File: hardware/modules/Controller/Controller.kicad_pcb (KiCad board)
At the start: 2 copper layers, 120 x 72 mm, 86 parts, among them J1 DEBUG, J2 Conn_01x04_MountingPin, J3 Jumper, J4 Conn_01x04_MountingPin, SW1 RESET, SW10 sw1, SW2 BOOT0, SW3 sw1, SW5 sw1, SW6 sw1, SW7 sw1, SW8 sw1, SW9 sw1, U1 SN65HVD230, U2 W25Q128JVS, U3 RP2040, Y1 Crystal_GND24

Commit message: 主にControllerの更新です
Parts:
- J2, J4: moved to F.Cu
- moved R1 56.5 mm to (122.3, 79.7)
- moved C12 56.5 mm to (110.9, 89.2)
- moved R12 56.4 mm to (121.2, 88.1)
- moved C11 56.4 mm to (121.2, 89.1)
- moved C15 56.4 mm to (111.0, 84.9)
- moved C3 56.4 mm to (113.5, 97.4)
- moved D2 56.4 mm to (112.1, 80.8)
- moved D3 56.4 mm to (116.1, 80.8)
- moved D4 56.4 mm to (118.2, 80.8)
- moved R10 56.4 mm to (122.5, 75.9)
- moved R4 56.4 mm to (114.3, 80.9)
- moved R9 56.4 mm to (118.0, 94.5)
- moved U1 56.4 mm to (127.0, 77.9)
- moved USB1 56.4 mm to (116.2, 75.1)
- moved C1 56.4 mm to (122.5, 77.8)
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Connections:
- C16 pad 2: /ModuleIF/VIO -> VDD
- J4 pad 3: /ModuleIF/VIO -> VDD
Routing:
- net GND: track 159.0 -> 433.7 mm, vias 12 -> 276
- net VDD: track 92.8 -> 323.5 mm
- net /raw2: track 0.00 -> 132.1 mm, vias 0 -> 5
- net /raw1: track 0.00 -> 125.7 mm, vias 0 -> 3
- net /raw4: track 0.00 -> 116.8 mm, vias 0 -> 1
- net Net-(lcd1-K): track 0.00 -> 116.1 mm, vias 0 -> 1
- net /raw3: track 0.00 -> 114.7 mm, vias 0 -> 1
- net /NoGo: track 0.00 -> 103.9 mm, vias 0 -> 4
- net /abort: track 0.00 -> 103.3 mm, vias 0 -> 4
- net /Go: track 0.00 -> 102.4 mm, vias 0 -> 4
- net /sub: track 0.00 -> 93.2 mm, vias 0 -> 5
- net /col4: track 0.00 -> 93.1 mm, vias 0 -> 2
- net /col3: track 0.00 -> 86.5 mm, vias 0 -> 2
- net /col2: track 0.00 -> 81.6 mm, vias 0 -> 2
- net /col1: track 0.00 -> 77.0 mm, vias 0 -> 2
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- added copper zone on B.Cu, net GND
- added copper zone on F.Cu, net GND

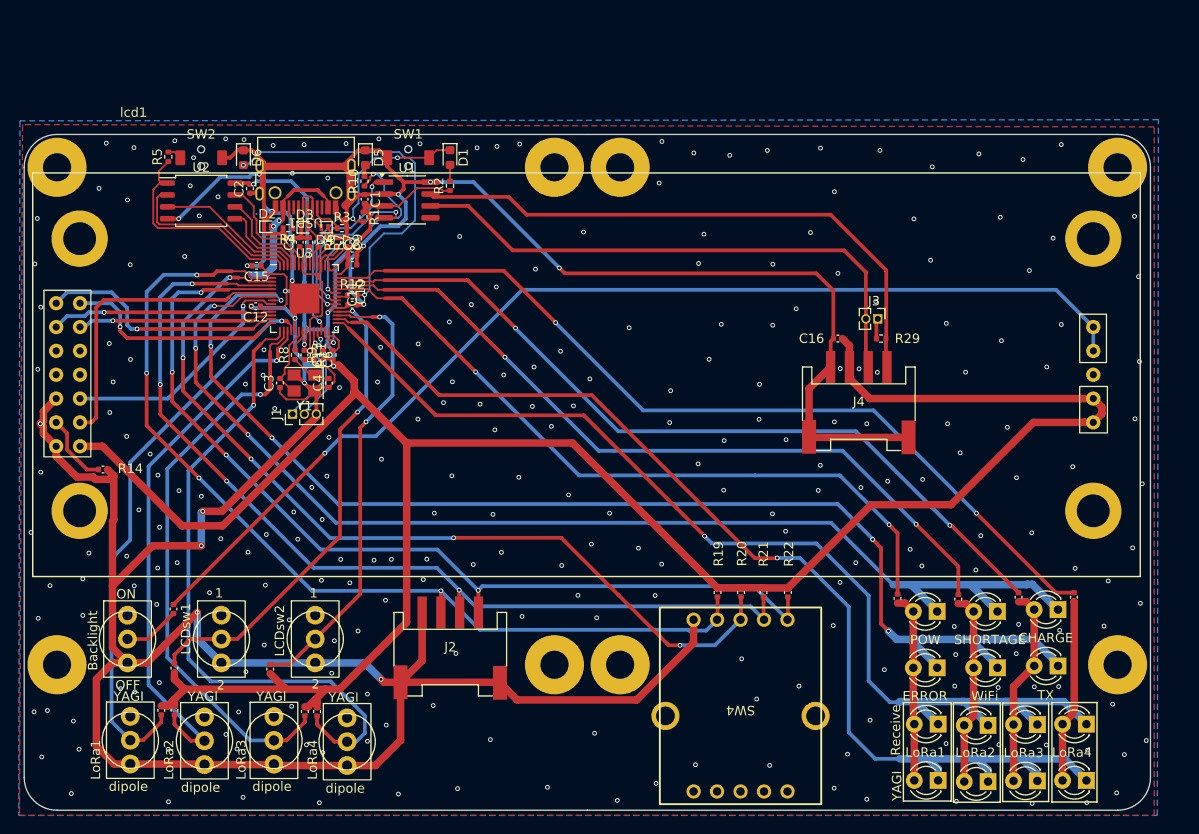
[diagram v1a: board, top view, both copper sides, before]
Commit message: Controllerの訂正です．レギュレータを追加追加したのと，差動通信線は平行にしてあります． 広範囲でベタをなくしたのは下層にＧＰＳアンテナがあるため削除したのですが，不必要ですか？確認お願いします．
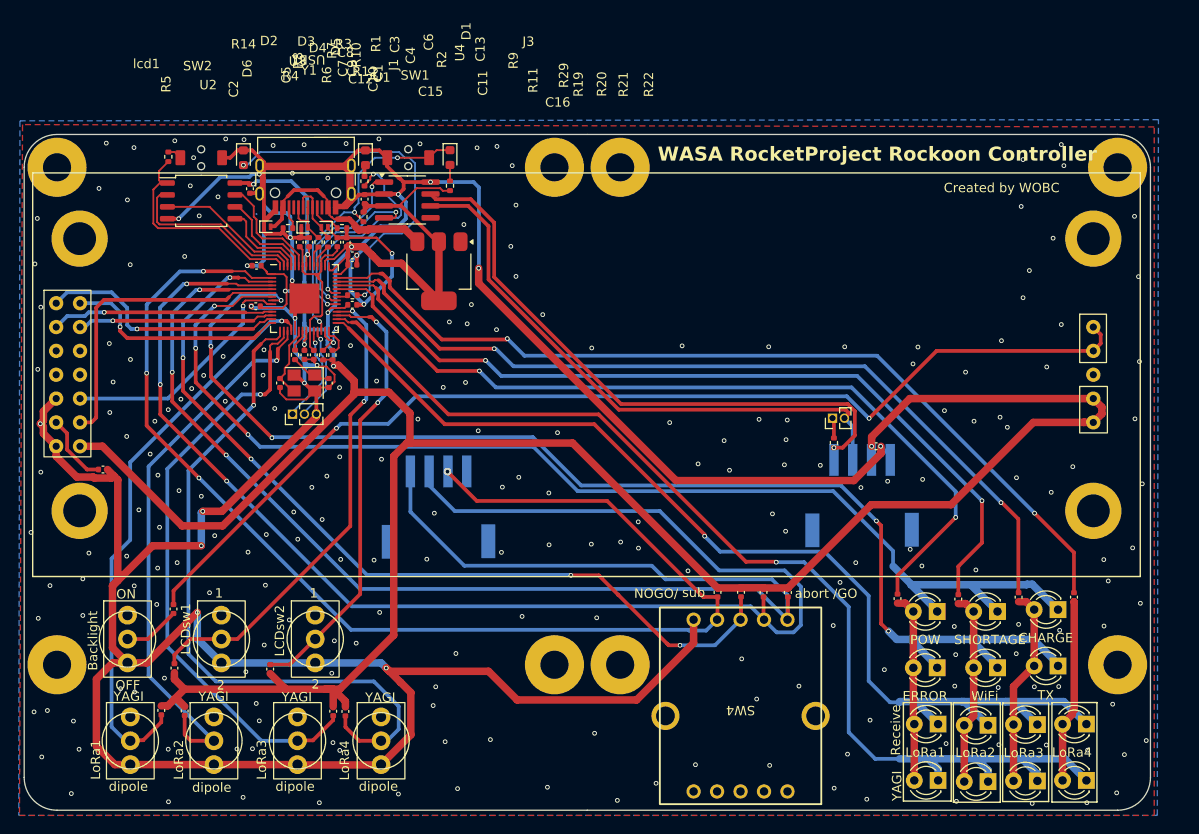
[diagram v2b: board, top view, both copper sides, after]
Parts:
- added U4: AMS1117-3.3, Package_TO_SOT_SMD:SOT-223-3_TabPin2, F.Cu at (130.4, 85.5)
- J2, J4: moved to B.Cu
- moved J2 15.1 mm to (130.3, 110.5), turned to 180 degrees
- moved R29 12.2 mm to (172.5, 103.8), turned to -90 degrees
- moved C16 12.2 mm to (177.0, 104.2), turned to 180 degrees
- moved J3 11.6 mm to (172.3, 101.2), turned to 90 degrees
- moved J4 9.91 mm to (175.5, 109.3), turned to 180 degrees
- moved SW6 3.62 mm to (124.2, 135.6)
- moved R27 3.02 mm to (119.1, 132.4)
- moved R28 3.02 mm to (120.4, 132.4)
- moved SW5 2.51 mm to (115.3, 135.6)
- moved R26 1.09 mm to (103.3, 132.4)
- moved SW8 1.01 mm to (106.4, 135.6)
- moved SW7 0.06 mm to (97.5, 135.6)
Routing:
- net /abort: track 103.3 -> 154.8 mm, vias 4 -> 3
- net /Go: track 102.4 -> 149.5 mm, vias 4 -> 3
- net /NoGo: track 103.9 -> 135.1 mm
- net VDD: track 323.5 -> 345.0 mm, vias 7 -> 8
- net /col1: track 77.0 -> 89.1 mm
- net /col2: track 81.6 -> 89.9 mm
- net /col3: track 86.5 -> 91.6 mm
- net VBUS: track 17.1 -> 21.9 mm, vias 2 -> 0
- net /LoRa4sw: track 70.0 -> 74.3 mm
- net /ModuleIF/CANL: track 59.5 -> 62.6 mm
- net /col4: track 93.1 -> 95.8 mm
- net /ModuleIF/CANH: track 62.3 -> 64.9 mm, vias 0 -> 1
- net /LoRa3sw: track 61.6 -> 63.8 mm
- net /raw2: track 132.1 -> 133.3 mm
- net /lcd_sw2: track 49.2 -> 48.2 mm
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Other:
- board text added: "/GO"
- board text added: "Created by WOBC"
- board text added: "GNG/NoGo/abort/Go"
- board text added: "GNG/VDD/CANL/CANH"
- board text added: "NOGO/"
- board text added: "WASA RocketProject Rockoon Controller"
- board text added: "abort"
- board text added: "sub"

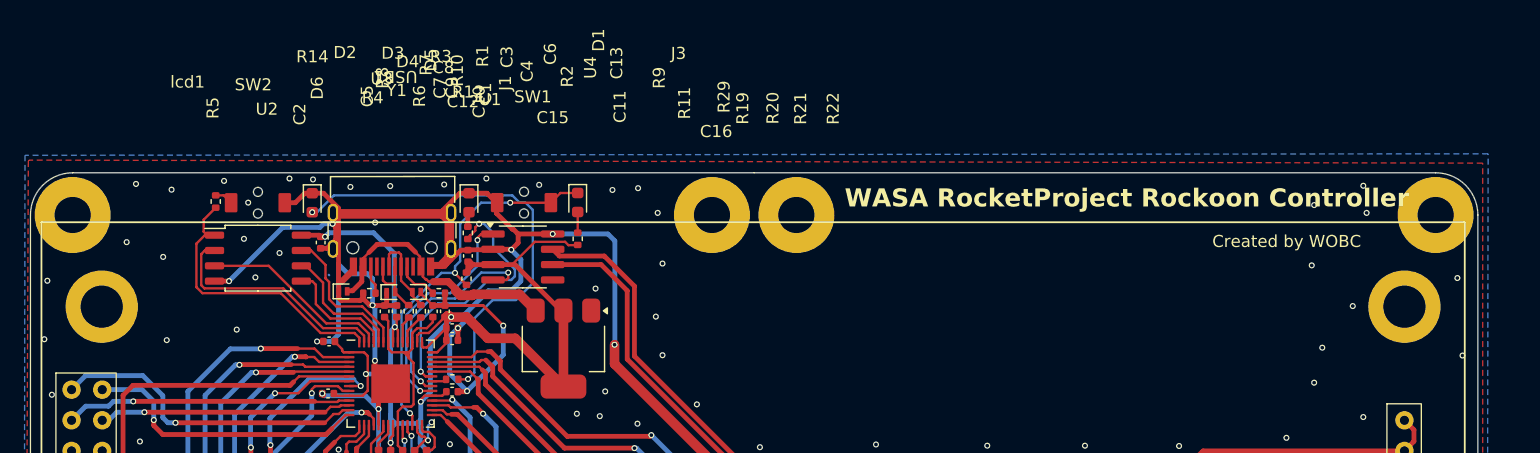
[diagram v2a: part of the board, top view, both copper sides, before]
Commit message: LoRaの全面的な配置変更，シルクを整えました．GSはこれで完了なのでWOBCの場で確認いただきたいです．
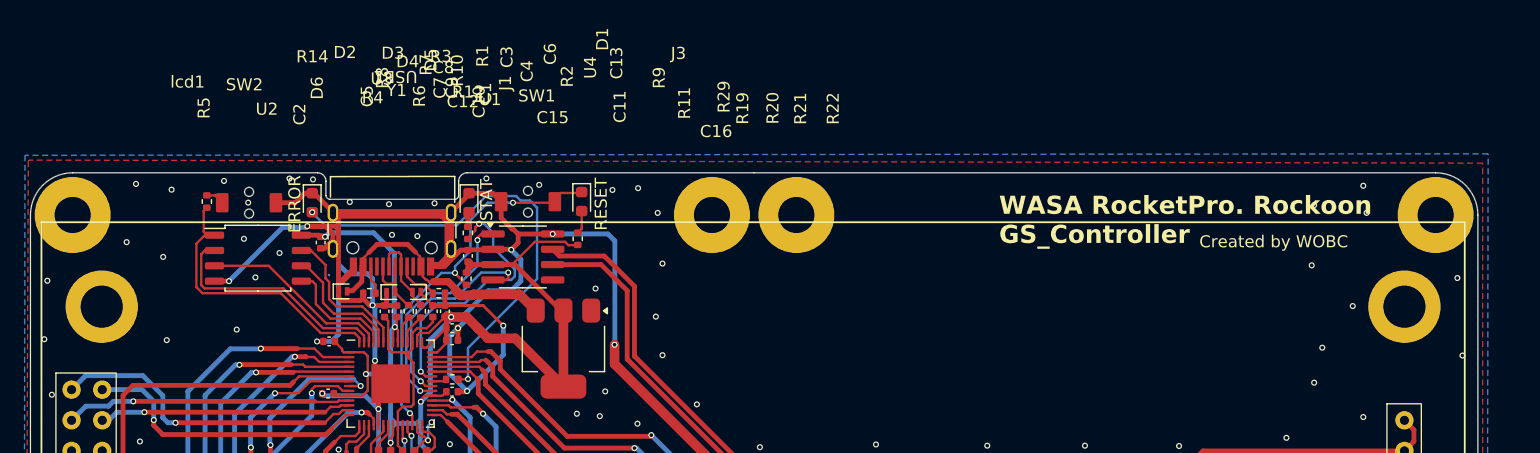
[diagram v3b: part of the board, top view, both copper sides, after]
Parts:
- moved R5 0.73 mm to (100.8, 73.3)
- moved SW2 0.73 mm to (104.3, 73.4)
- moved D1 0.34 mm to (131.9, 73.3)
- moved SW1 0.34 mm to (127.5, 73.3)
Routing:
- net GND: track 434.3 -> 436.0 mm
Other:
- outline, holes or cut-outs redrawn
- board text added: "RESET"
- board text added: "STAT"
- board text added: "WASA RocketPro. Rockoon GS_Controller"
- board text removed: "WASA RocketProject Rockoon Controller"

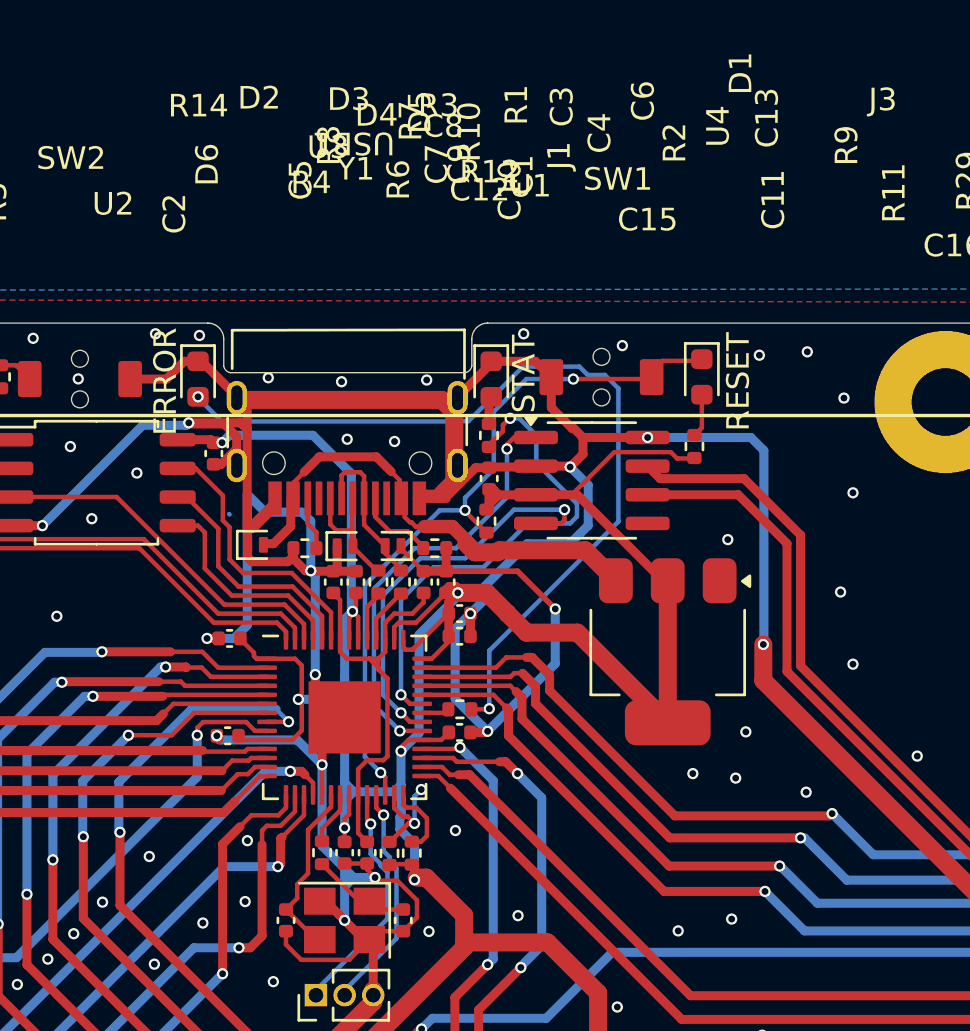
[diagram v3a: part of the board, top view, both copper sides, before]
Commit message: GSモジュール一式完成です．最終確認をお願いします．週末に発注しようと思います．
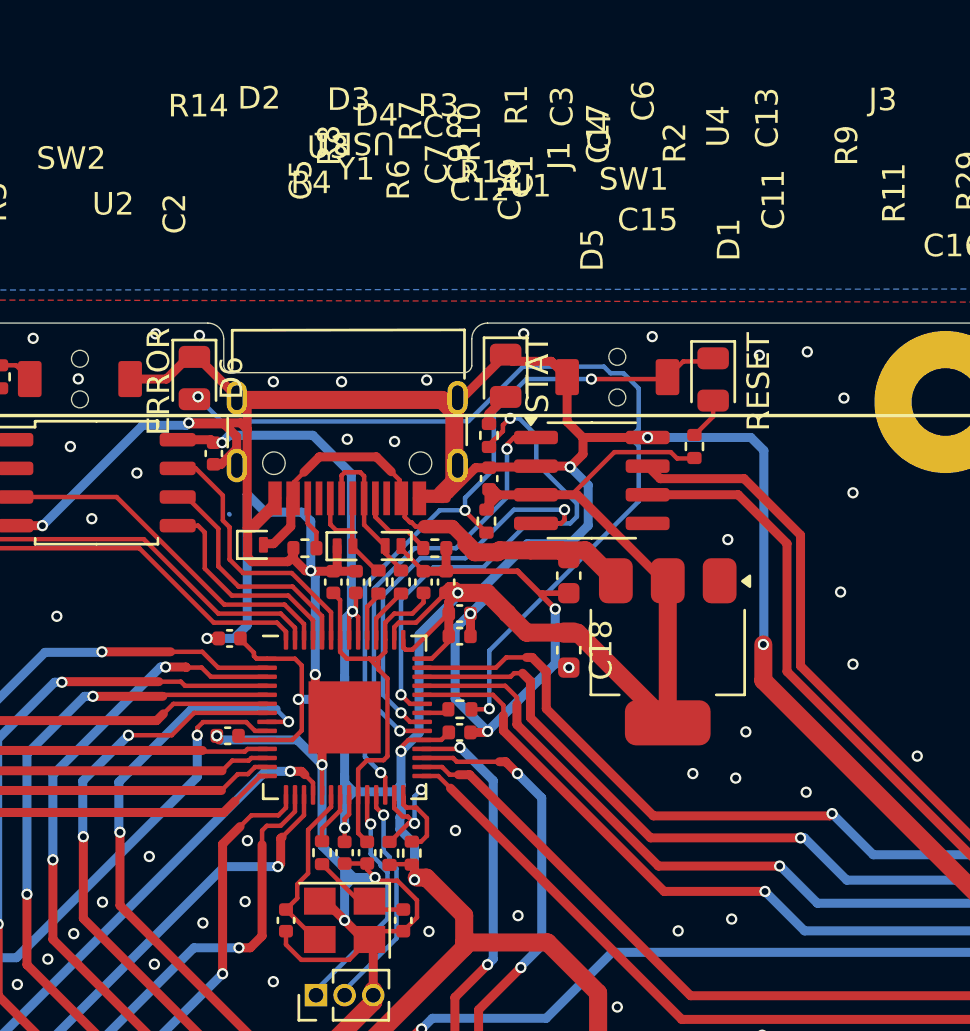
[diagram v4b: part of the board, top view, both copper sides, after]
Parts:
- added C17: 10u, Capacitor_SMD:C_0603_1608Metric, F.Cu at (126.0, 82.2)
- added C18: 10u, Capacitor_SMD:C_0603_1608Metric, F.Cu at (126.0, 85.5)
- D1, D5, D6: footprint LED_SMD:LED_0603_1608Metric -> LED_SMD:LED_0805_2012Metric
- moved SW1 0.70 mm to (128.2, 73.3)
- moved D5 0.66 mm to (123.2, 73.3)
- moved D1 0.51 mm to (132.4, 73.5)
- moved D6 0.17 mm to (109.4, 73.4)
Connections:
- REF** pad GND: (no net) -> GND
- lcd1 pad GND: (no net) -> GND
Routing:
- net GND: track 436.0 -> 438.5 mm, vias 248 -> 249
- net VBUS: track 21.9 -> 23.8 mm
- net Net-(D6-A): track 37.9 -> 39.3 mm
- net RESET: track 31.6 -> 32.5 mm
- net /col4: track 95.8 -> 96.4 mm
- net VDD: track 345.0 -> 345.5 mm

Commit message: 各コンポーネントの修正をしました．一度プッシュします(多分コンフリクトするので)．
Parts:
- SW101: renamed from SW1; value RESET -> RESET_sw
- renumbered C17 to C101, C18 to C102, C1 to C103, C2 to C104, C3 to C105, C4 to C106, C5 to C107, C6 to C108, C7 to C109, C8 to C110, C9 to C111, C10 to C112, C11 to C113, C12 to C114, C13 to C115, C14 to C116, C15 to C117, C16 to C118, D1 to D101, D2 to D102, D3 to D103, D4 to D104, D5 to D105, D6 to D106, D7 to D107, D8 to D108, D9 to D109, D10 to D110, D11 to D111, D12 to D112, D13 to D113, D14 to D114, D15 to D115, D16 to D116, D17 to D117, D18 to D118, D19 to D119, D20 to D120, J1 to J101, J2 to J102, J3 to J103, J4 to J104, R1 to R101, R2 to R102, R3 to R103, R4 to R104, R5 to R105, R6 to R106, R7 to R107, R8 to R108, R9 to R109, R10 to R110, R11 to R111, R12 to R112, R13 to R113, R14 to R114, R15 to R115, R16 to R116, R17 to R117, R18 to R118, R19 to R119, R20 to R120, R21 to R121, R22 to R122, R23 to R123, R24 to R124, R25 to R125, R26 to R126, R27 to R127, R28 to R128, R29 to R129, SW2 to SW102, SW3 to SW103, SW4 to SW104, SW5 to SW105, SW6 to SW106, SW7 to SW107, SW8 to SW108, SW9 to SW109, SW10 to SW110, U4 to U101, U1 to U102, U2 to U103, U3 to U104, USB1 to USB101, Y1 to Y101, lcd1 to lcd101
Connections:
- lcd101 pad GND: GND -> (no net)

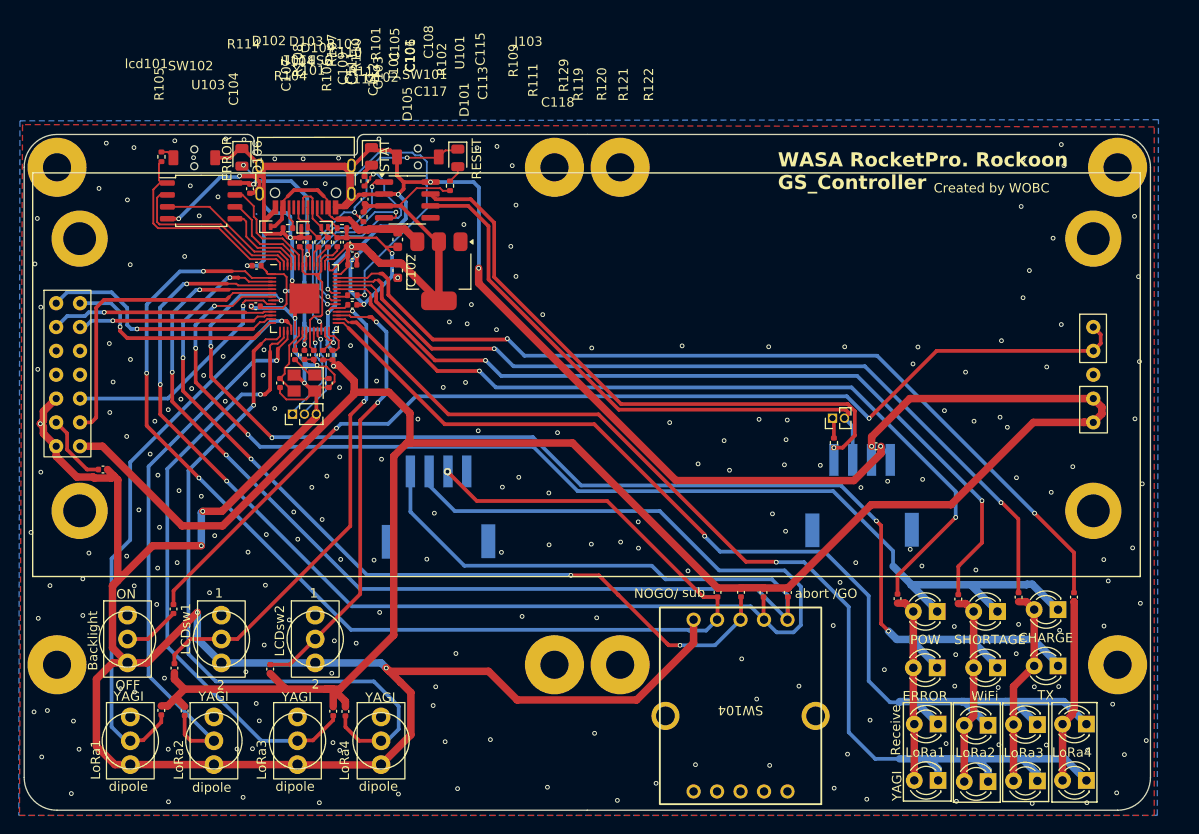
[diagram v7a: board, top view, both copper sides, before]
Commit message: Controllet基板一部修正です、LCDのピン配置ミスってて修正も難しいのでLCDのるもののみ再発注する予定です。
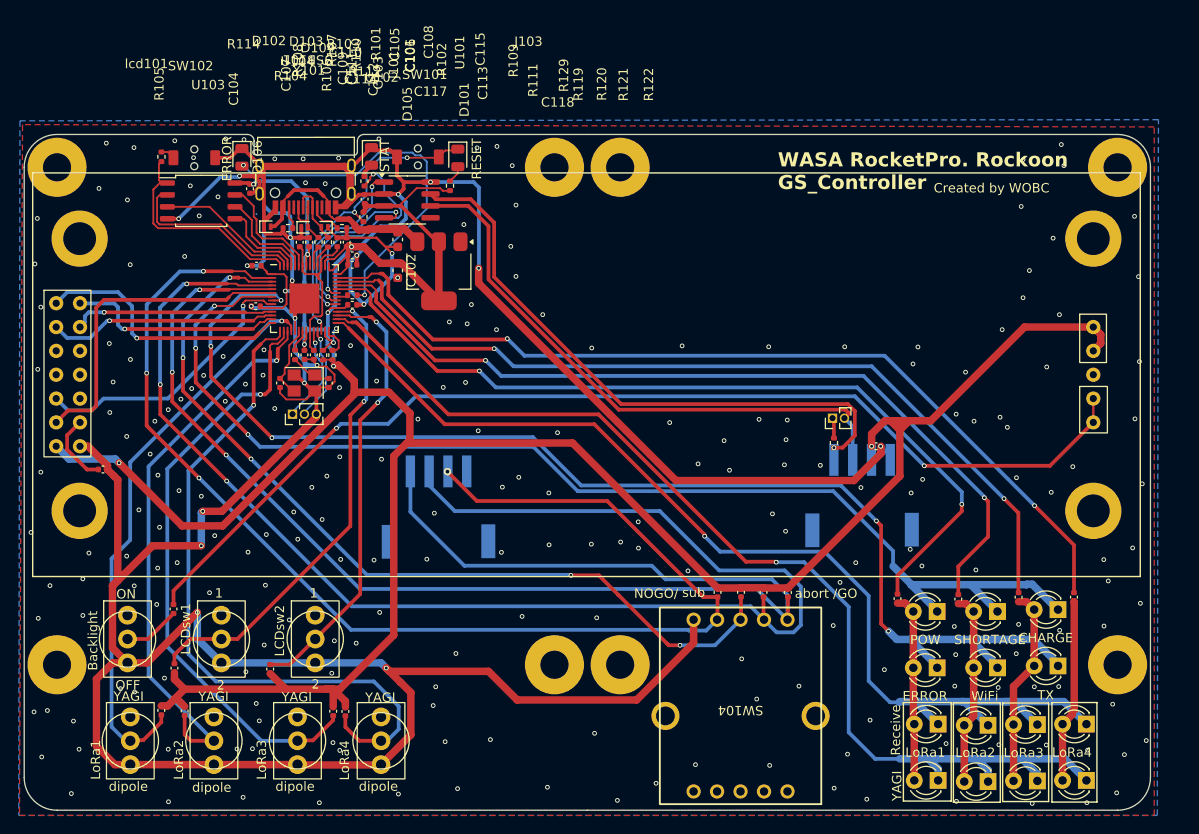
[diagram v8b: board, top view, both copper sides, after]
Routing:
- net GND: track 438.5 -> 428.0 mm, vias 249 -> 248
- net VDD: track 345.5 -> 336.0 mm, vias 8 -> 9
- net /DB7: track 23.9 -> 27.9 mm
- net /E: track 26.2 -> 29.8 mm
- net /DB5: track 21.0 -> 24.5 mm
- net /DB6: track 26.6 -> 23.2 mm
- net /DB4: track 23.7 -> 21.6 mm
- net /RS: track 33.1 -> 34.9 mm
- net /col2: track 90.0 -> 90.9 mm
- net /col1: track 89.0 -> 89.9 mm
